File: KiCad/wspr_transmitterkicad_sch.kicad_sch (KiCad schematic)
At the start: 9 parts, among them U4 Si5351A-B-GT, U9 TPS2552DRVR, X2 X1G0042110003_C3013793

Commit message: Start of docs and design incremental progress
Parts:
- U4: footprint JetBoard:SOIC-8_L5.3-W5.3-P1.27-LS8.0-BL -> Package_SO:MSOP-10_3x3mm_P0.5mm
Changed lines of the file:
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@@
 			)
 		)
-		(property "Footprint" "JetBoard:SOIC-8_L5.3-W5.3-P1.27-LS8.0-BL"
+		(property "Footprint" "Package_SO:MSOP-10_3x3mm_P0.5mm"
 			(at 123.19 78.74 0)
 			(effects

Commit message: Update schematic and board
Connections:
- net +3.3V_WSPR: no longer C31.1, C32.1, C33.1, U9.1 (OUT)
- net +3.3V renamed +3V3
- new net +3V3_WSPR: C31.1, C32.1, C33.1, U9.1 (OUT)
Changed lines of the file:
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@@
 			)
 		)
-		(property "Value" "+3.3V_WSPR"
-			(at 78.74 20.32 0)
-			(effects
-				(font
-					(size 1.27 1.27)
-				)
+		(property "Value" "+3V3_WSPR"
+			(at 81.28 24.1299 0)
+			(effects
+				(font
+					(size 1.27 1.27)
+				)
+				(justify left)
 			)
 		)
@@
 			)
 		)
-		(property "Value" "+3.3V_WSPR"
-			(at 152.4 22.86 0)
-			(effects
-				(font
-					(size 1.27 1.27)
-				)
+		(property "Value" "+3V3_WSPR"
+			(at 154.94 26.6699 0)
+			(effects
+				(font
+					(size 1.27 1.27)
+				)
+				(justify left)
 			)
 		)
@@
 			)
 		)
-		(property "Value" "+3.3V"
-			(at 39.37 20.32 0)
-			(effects
-				(font
-					(size 1.27 1.27)
-				)
-			)
-		)
+		(property "Value" "+3V3"
+			(at 41.91 24.1299 0)
+			(effects
+				(font
+					(size 1.27 1.27)
+				)
+				(justify left)
+			)
+		)

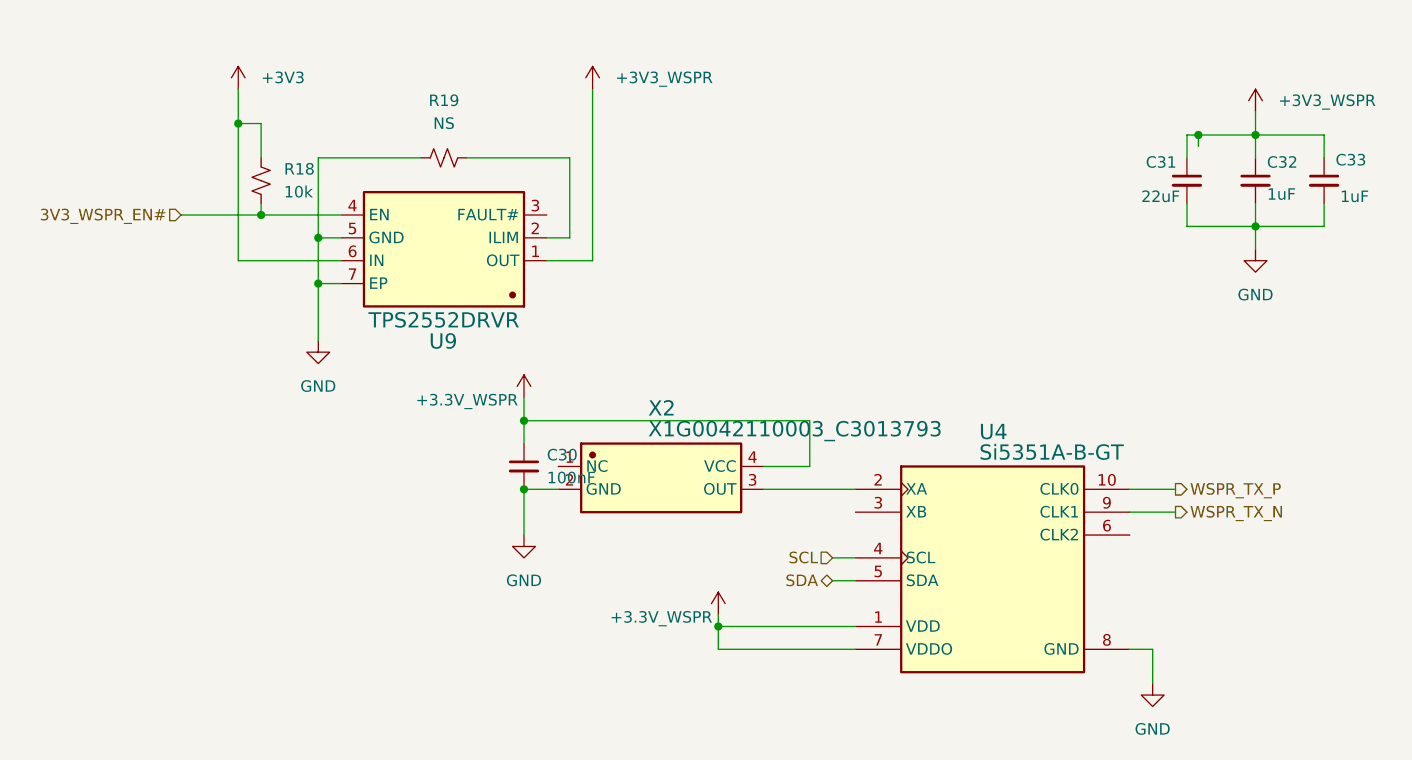
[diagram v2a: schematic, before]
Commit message: 3D model fixes and change to 3.0V buck
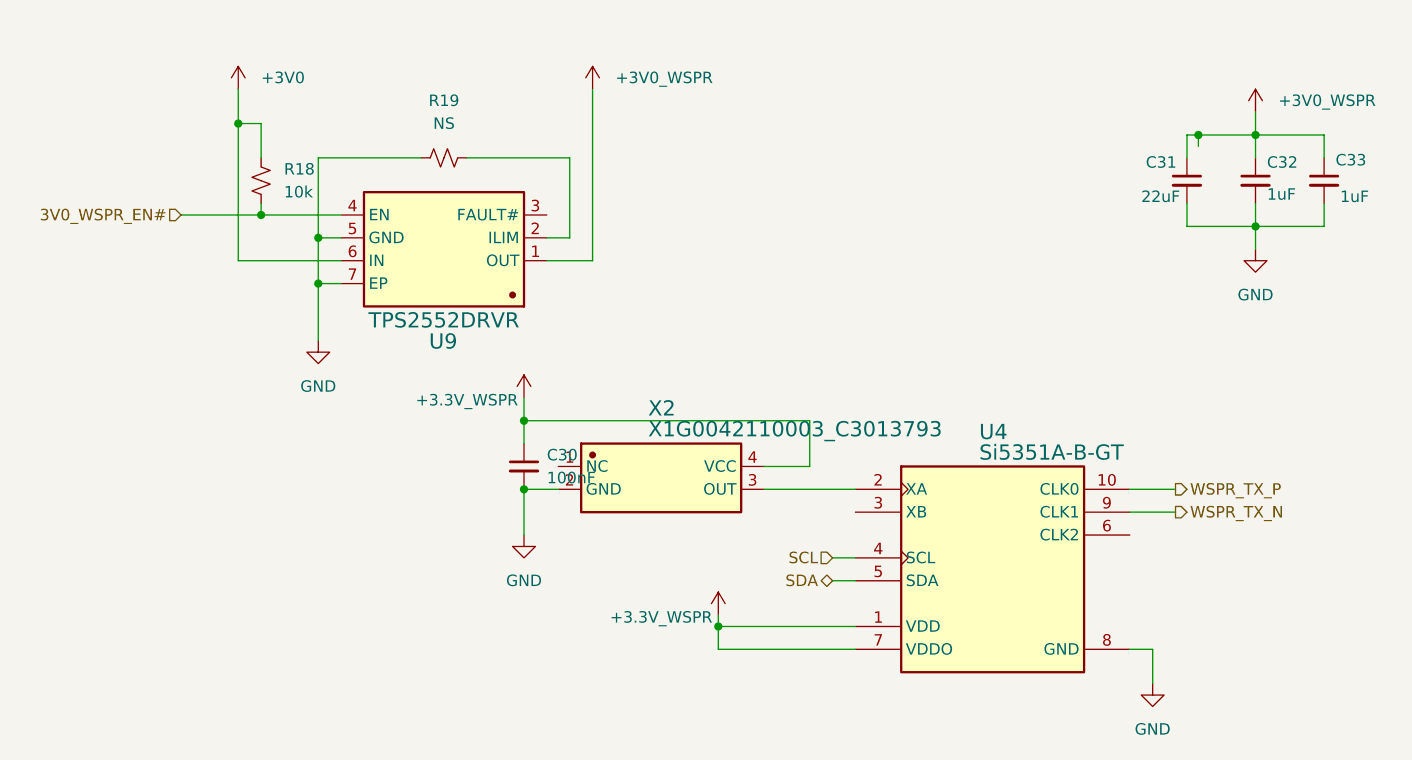
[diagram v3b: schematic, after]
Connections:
- net +3V3 renamed +3V0
- net +3V3_WSPR renamed +3V0_WSPR
- net 3V3_WSPR_EN# renamed 3V0_WSPR_EN#
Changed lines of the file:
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@@
 		)
 	)
-	(hierarchical_label "3V3_WSPR_EN#"
+	(hierarchical_label "3V0_WSPR_EN#"
 		(shape input)
 		(at 33.02 39.37 180)
@@
 			)
 		)
-		(property "Value" "+3V3_WSPR"
+		(property "Value" "+3V0_WSPR"
 			(at 81.28 24.1299 0)
 			(effects
@@
 			)
 		)
-		(property "Value" "+3V3_WSPR"
+		(property "Value" "+3V0_WSPR"
 			(at 154.94 26.6699 0)
 			(effects
@@
 			)
 		)
-		(property "Value" "+3V3"
+		(property "Value" "+3V0"
 			(at 41.91 24.1299 0)
 			(effects

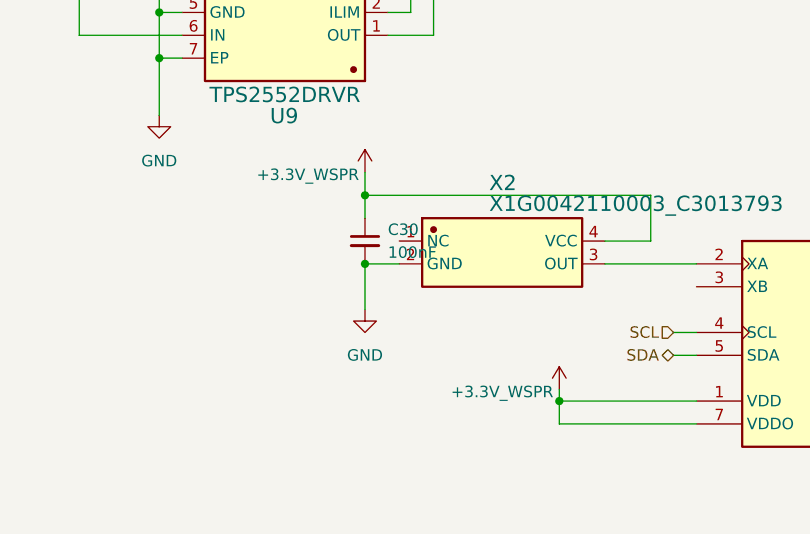
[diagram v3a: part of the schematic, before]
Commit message: Schematic changes
- Changed to STM8L050
- Changed to SPI interface for STM8 bootloader
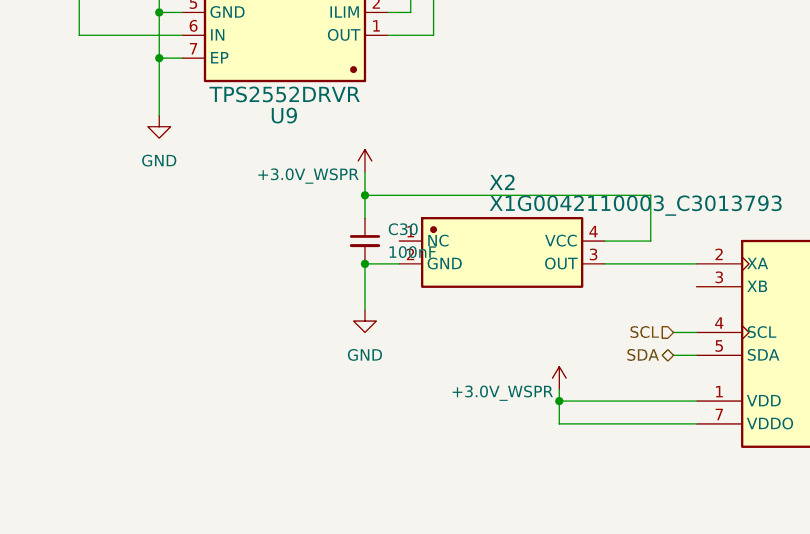
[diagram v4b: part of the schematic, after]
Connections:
- net +3.3V_WSPR renamed +3.0V_WSPR
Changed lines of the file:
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@@
 			)
 		)
-		(property "Value" "+3.3V_WSPR"
+		(property "Value" "+3.0V_WSPR"
 			(at 86.36 84.074 0)
 			(effects
@@
 			)
 		)
-		(property "Value" "+3.3V_WSPR"
+		(property "Value" "+3.0V_WSPR"
 			(at 64.77 59.944 0)
 			(effects

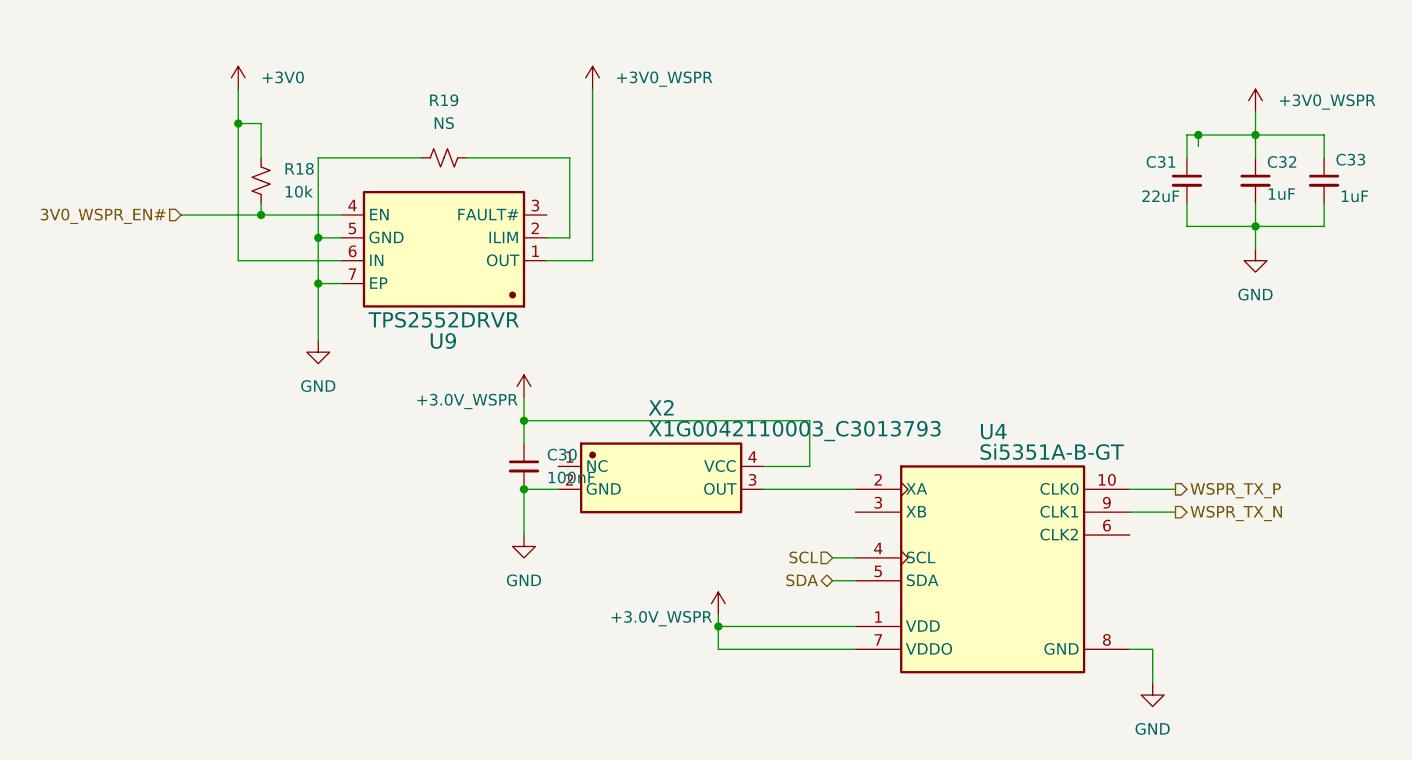
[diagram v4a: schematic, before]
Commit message: Clean up ERC errors
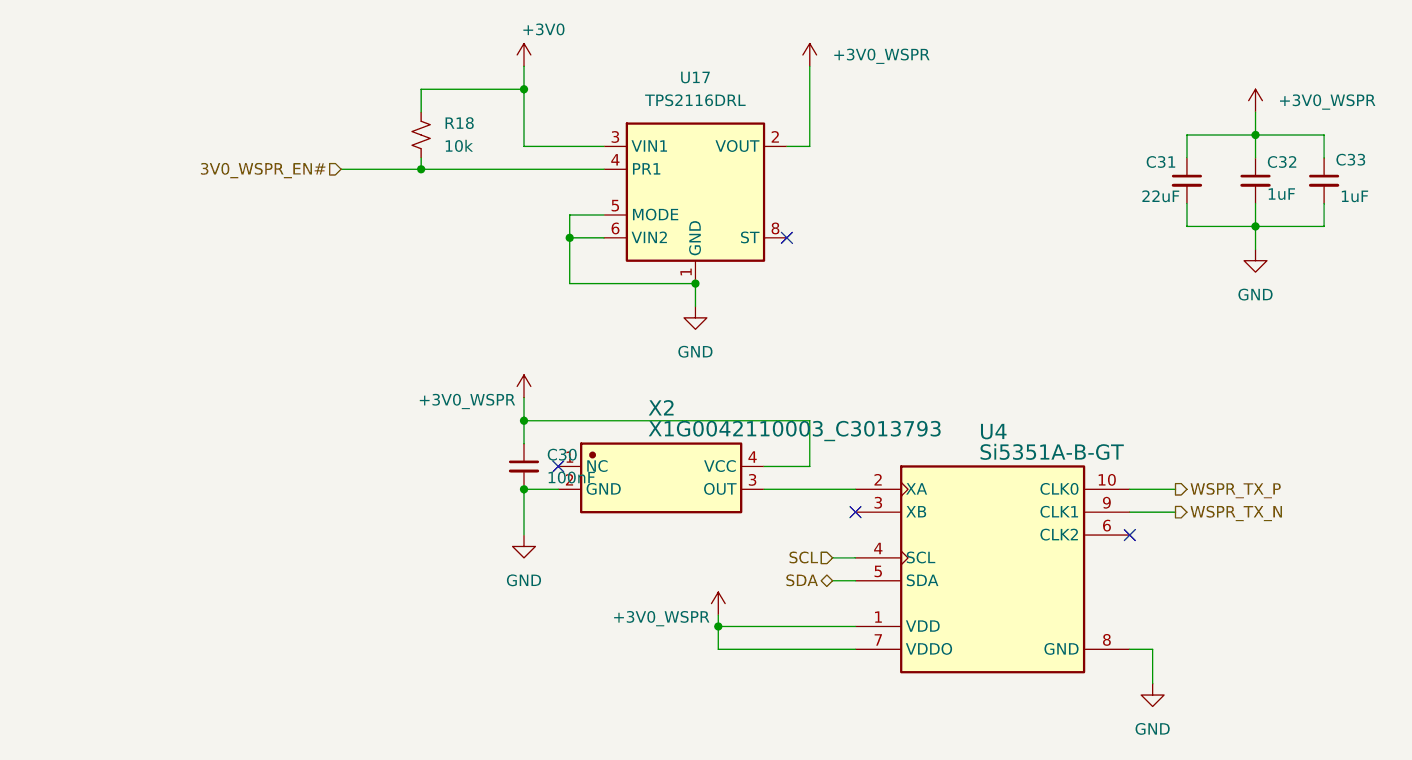
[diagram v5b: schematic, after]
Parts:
- removed R19: NS, Resistor_SMD:R_0402_1005Metric, symbol Device:R_Small_US
- removed U9: TPS2552DRVR, JetBoard:WSON-6_L2.0-W2.0-P0.65-TL-EP, symbol TPS2552DRVR
- added U17: TPS2116DRL, Package_TO_SOT_SMD:SOT-583-8, symbol Power_Management:TPS2116DRL
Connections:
- net +3.0V_WSPR is gone; now on net +3V0_WSPR: C30.1, U4.1 (VDD), U4.7 (VDDO), X2.4 (VCC)
- net +3V0: now also R18.2, U17.3 (VIN1); no longer R18.1
- net +3V0_WSPR: now also U17.2 (VOUT), U17.7 (VOUT)
- net 3V0_WSPR_EN#: now also R18.1, U17.4 (PR1); no longer R18.2
- net GND: now also U17.1 (GND), U17.5 (MODE), U17.6 (VIN2)
- no-connect marks 0 -> 4
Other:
- moved on the sheet: R18

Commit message: DRC cleanup
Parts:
- added R25, R26: 5.1k, Resistor_SMD:R_0402_1005Metric, symbol Device:R_Small_US
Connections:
- net +3V0_WSPR: now also R25.2, R26.2
- net SCL: now also R25.1
- net SDA: now also R26.1

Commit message: Mods
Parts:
- U4: symbol Si5351A-B-GT -> JetBoard:Si5351A-B-GT
- X2: symbol X1G0042110003_C3013793 -> JetBoard:X1G0042110003_C3013793
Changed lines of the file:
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@@
 	)
 	(symbol
-		(lib_id "X1G0042110003_C3013793")
+		(lib_id "JetBoard:X1G0042110003_C3013793")
 		(at 87.63 69.85 0)
 		(unit 1)
@@
 	)
 	(symbol
-		(lib_id "Si5351A-B-GT")
+		(lib_id "JetBoard:Si5351A-B-GT")
 		(at 123.19 78.74 0)
 		(unit 1)
